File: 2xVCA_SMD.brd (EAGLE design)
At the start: 100 x 29.2 mm, 50 parts, among them IC1 TL072D, IC2 LM13700M, IC3 TL072D, Q1 MMBT3906LT1SMD, Q2 MMBT3906LT1SMD, Q4 BC847SMD, Q5 BC847SMD

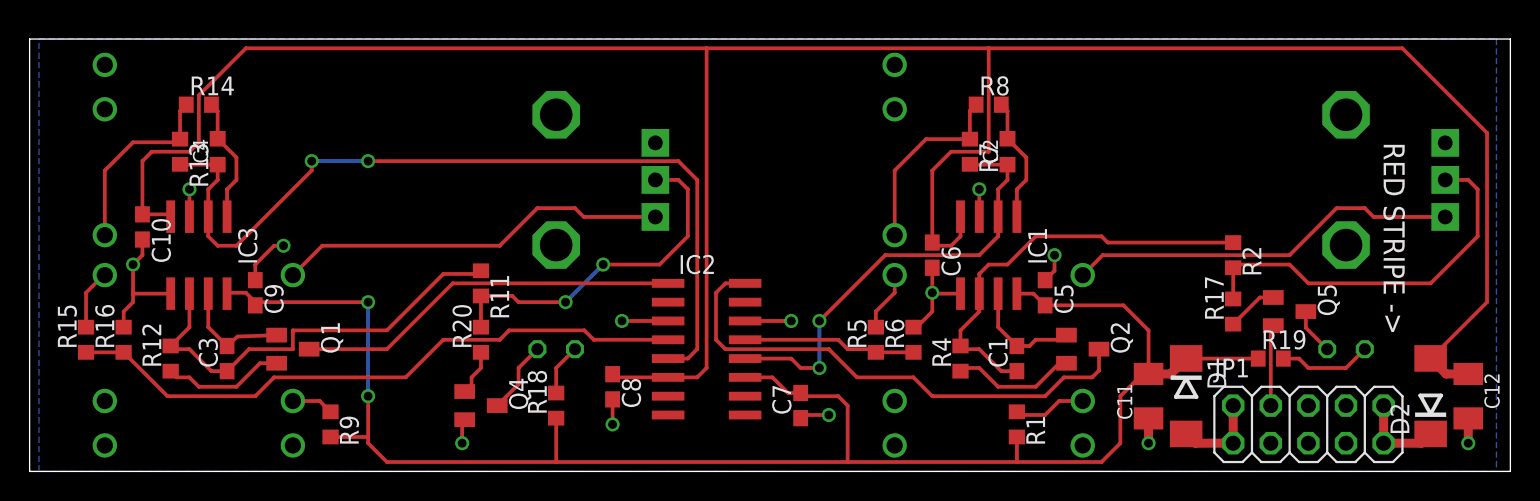
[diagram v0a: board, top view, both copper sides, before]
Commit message: Fixed component labels. Minor routing adjustments. Spread PSU components a bit. Added board type label & copyright notice.
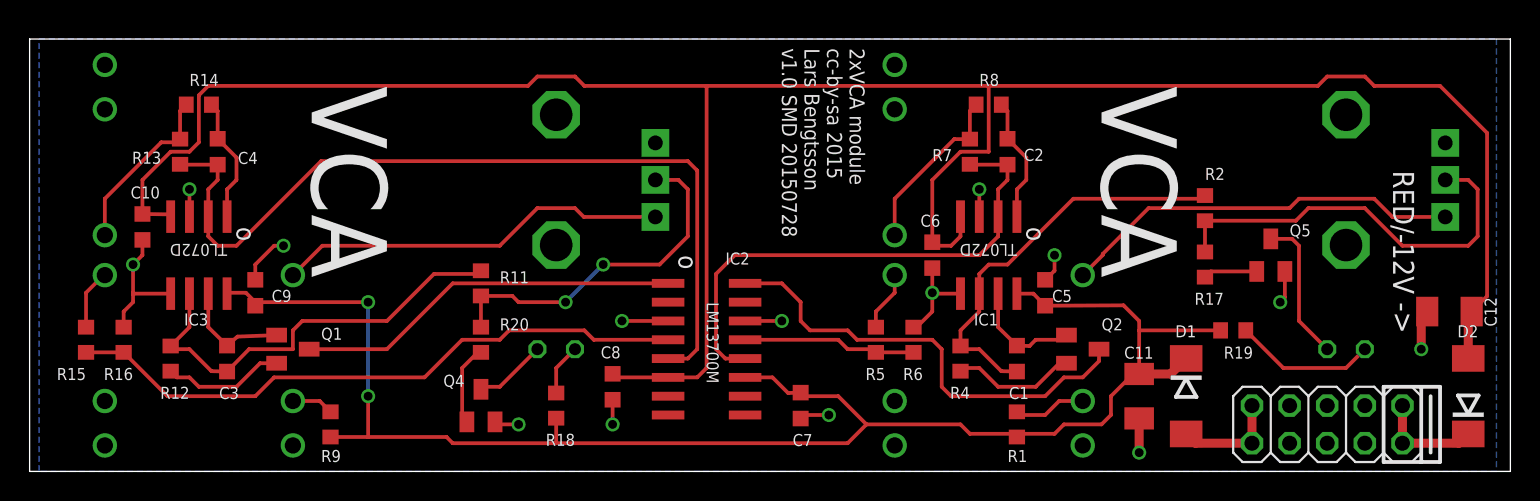
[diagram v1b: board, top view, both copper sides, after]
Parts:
- C1, C10, C3, C5, C6, C7, C8, C9: device rcl:C0603 -> rcl:C0603K
- moved C12 5.85 mm to (95.9, 16.5), turned to 180 degrees
- moved Q5 4.02 mm to (83.8, 20.3), turned to 0 degrees
- moved R2 3.70 mm to (79.4, 23.5)
- moved R17 3.70 mm to (79.4, 19.7)
- moved R19 3.17 mm to (81.3, 15.2)
- moved D2 2.54 mm to (97.2, 10.8)
- moved JP1 1.27 mm to (87.6, 8.89)
- moved C11 0.63 mm to (74.9, 10.8)
- turned Q4 to 0 degrees
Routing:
- net VSS: track 171.6 -> 160.3 mm
- net N$24: track 3.14 -> 9.87 mm
- net VCC: track 116.7 -> 110.4 mm
- net N$6: track 30.5 -> 35.1 mm, vias 2 -> 0
- net I_VCA1: track 35.0 -> 31.1 mm
- net N$18: track 6.29 -> 9.62 mm
- net N$27: track 3.10 -> 5.48 mm
- net GND: track 45.1 -> 42.8 mm, vias 13 -> 14
- net CV_ATT_1: track 26.2 -> 27.8 mm
- net N$30: track 5.97 -> 7.24 mm
- net N$28: track 5.97 -> 7.24 mm
- net N$20: track 12.8 -> 11.7 mm
- net N$13: track 12.8 -> 11.7 mm
- net N$5: track 28.3 -> 27.3 mm
- net N$3: track 26.6 -> 27.2 mm
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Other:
- board text added: "2xVCA module cc-by-sa 2015 Lars Bengtsson v1.0 SMD 20150728"
- board text added: "RED/-12V ->"
- board text added: "VCA"
- board text added: "o"
- board text removed: "RED STRIPE ->"

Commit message: Minor routing fixes. Adjusted labels a bit.
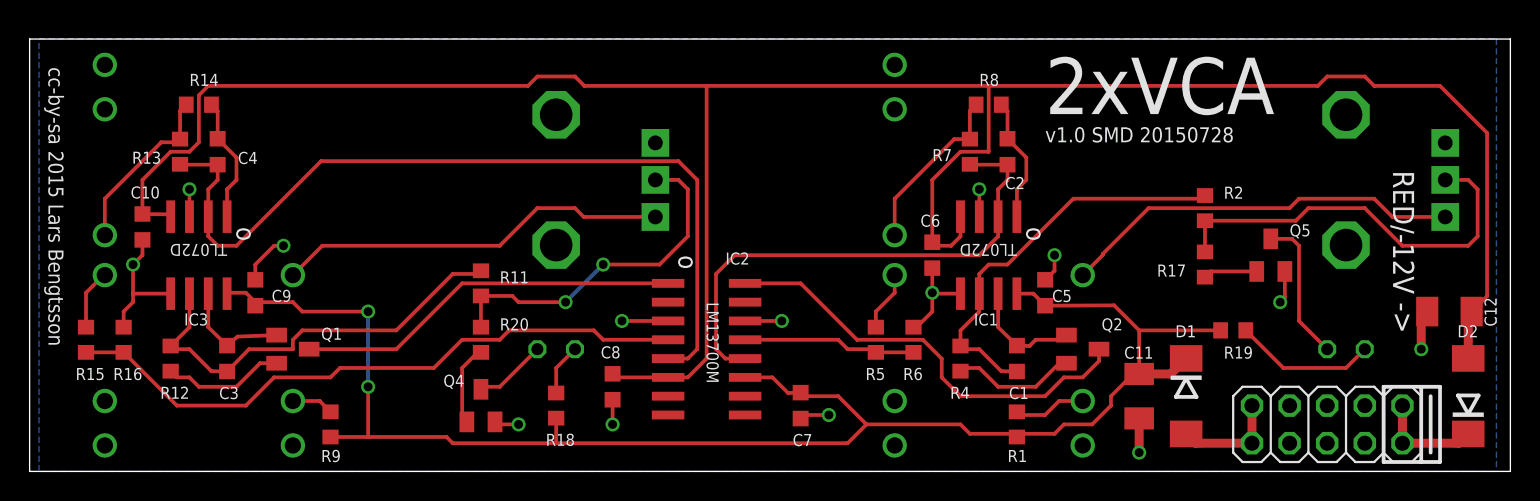
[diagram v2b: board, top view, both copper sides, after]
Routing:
- net I_VCA1: track 31.1 -> 29.6 mm
- net VCC: track 110.4 -> 109.3 mm
- net N$10: track 42.6 -> 43.2 mm
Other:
- board text added: "2xVCA"
- board text added: "cc-by-sa 2015 Lars Bengtsson"
- board text added: "v1.0 SMD 20150728"
- board text removed: "2xVCA module cc-by-sa 2015 Lars Bengtsson v1.0 SMD 20150728"
- board text removed: "VCA"

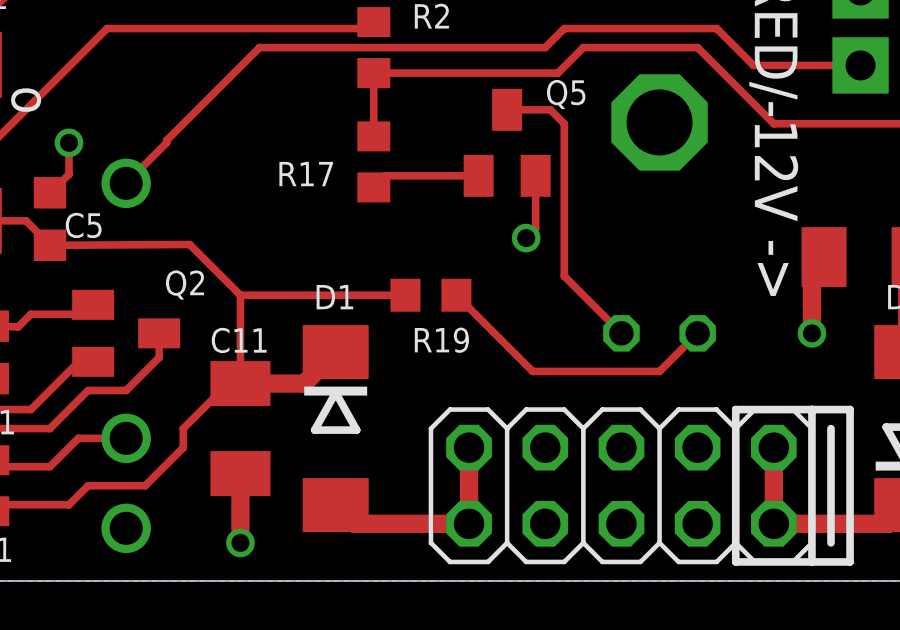
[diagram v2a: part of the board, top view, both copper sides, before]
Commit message: Rotated T19 to match the rest :)
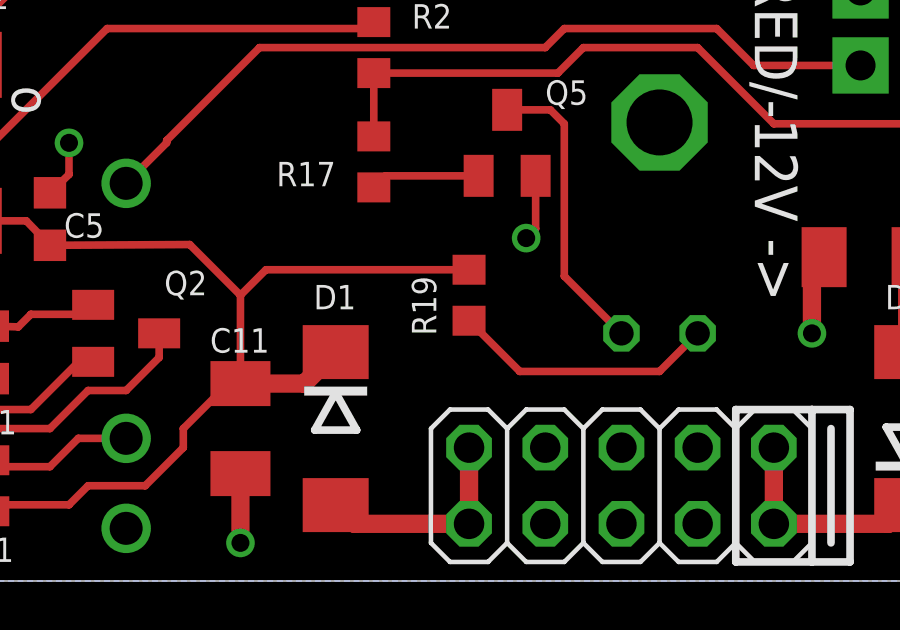
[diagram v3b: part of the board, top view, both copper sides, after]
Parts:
- moved R19 1.27 mm to (82.5, 15.2), turned to 270 degrees
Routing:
- net VCC: track 109.3 -> 111.8 mm
- net N$18: track 9.62 -> 8.85 mm
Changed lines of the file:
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@@
 <attribute name="VALUE" x="37.465" y="9.525" size="1.27" layer="27" rot="R90"/>
 </element>
-<element name="R19" library="rcl" package="R0603" value="10k" x="81.28" y="15.24" smashed="yes">
-<attribute name="NAME" x="80.645" y="13.335" size="0.8128" layer="25" font="vector"/>
-<attribute name="VALUE" x="80.645" y="13.335" size="1.27" layer="27"/>
+<element name="R19" library="rcl" package="R0603" value="10k" x="82.55" y="15.24" smashed="yes" rot="R270">
+<attribute name="NAME" x="80.645" y="15.875" size="0.8128" layer="25" font="vector" rot="R270"/>
+<attribute name="VALUE" x="80.645" y="15.875" size="1.27" layer="27" rot="R270"/>
 </element>
 <element name="R2" library="rcl" package="R0603" value="33k" x="79.375" y="23.495" smashed="yes" rot="R270">
@@
 <wire x1="74.93" y1="12.295" x2="74.525" y2="12.295" width="0.254" layer="1"/>
 <wire x1="74.525" y1="12.295" x2="73.025" y2="10.795" width="0.254" layer="1"/>
-<wire x1="80.43" y1="15.24" x2="74.93" y2="15.24" width="0.254" layer="1"/>
 <wire x1="20.32" y1="8.04" x2="22.86" y2="8.04" width="0.254" layer="1"/>
 <wire x1="22.86" y1="8.04" x2="22.86" y2="11.43" width="0.254" layer="1"/>
@@
 <wire x1="54.61" y1="10.795" x2="56.515" y2="8.89" width="0.254" layer="1"/>
 <wire x1="35.56" y1="9.31" x2="35.56" y2="7.62" width="0.254" layer="1"/>
+<wire x1="82.55" y1="16.09" x2="75.78" y2="16.09" width="0.254" layer="1"/>
+<wire x1="75.78" y1="16.09" x2="74.93" y2="15.24" width="0.254" layer="1"/>
 </signal>
 <signal name="N$16">
@@
 <contactref element="LED1" pad="A"/>
 <wire x1="90.17" y1="13.97" x2="88.9" y2="12.7" width="0.254" layer="1"/>
-<wire x1="88.9" y1="12.7" x2="84.67" y2="12.7" width="0.254" layer="1"/>
-<wire x1="84.67" y1="12.7" x2="82.13" y2="15.24" width="0.254" layer="1"/>
+<wire x1="88.9" y1="12.7" x2="84.24" y2="12.7" width="0.254" layer="1"/>
+<wire x1="84.24" y1="12.7" x2="82.55" y2="14.39" width="0.254" layer="1"/>
 </signal>
 <signal name="N$24">
